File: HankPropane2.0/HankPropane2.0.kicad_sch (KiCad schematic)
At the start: 3 parts, among them X1 Badgelife_sao_connector_v169b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

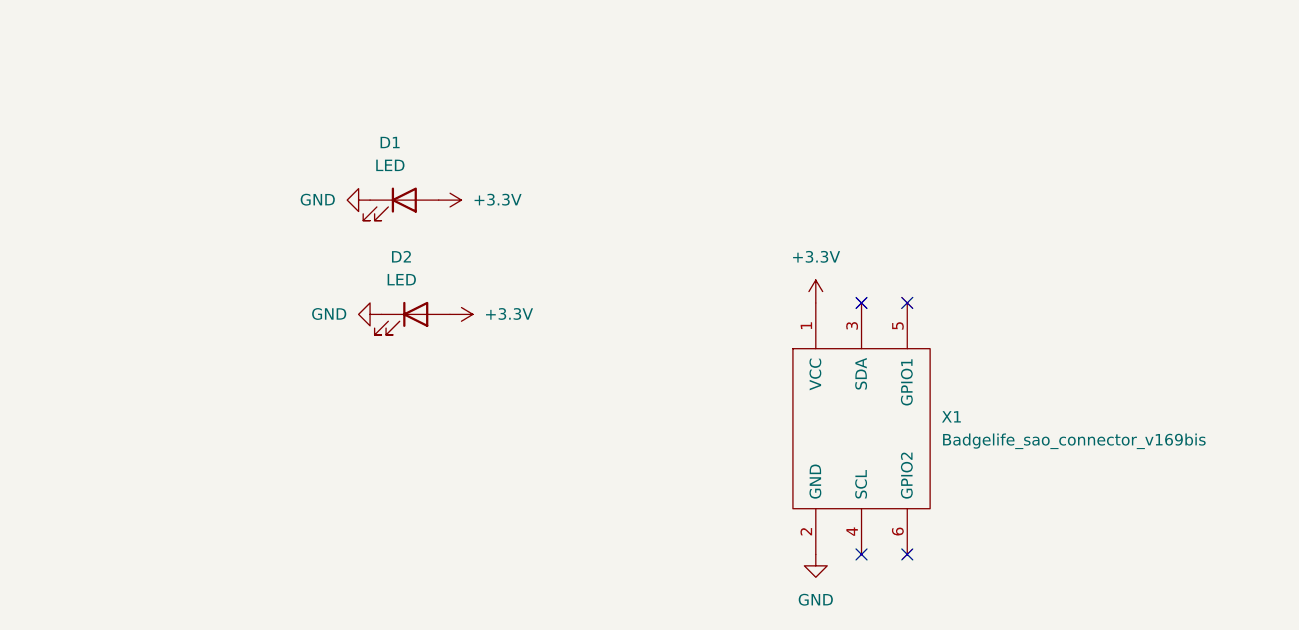
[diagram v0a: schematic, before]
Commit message: Added 68.1 ohm current limiting resistors and turbo mode jumpers
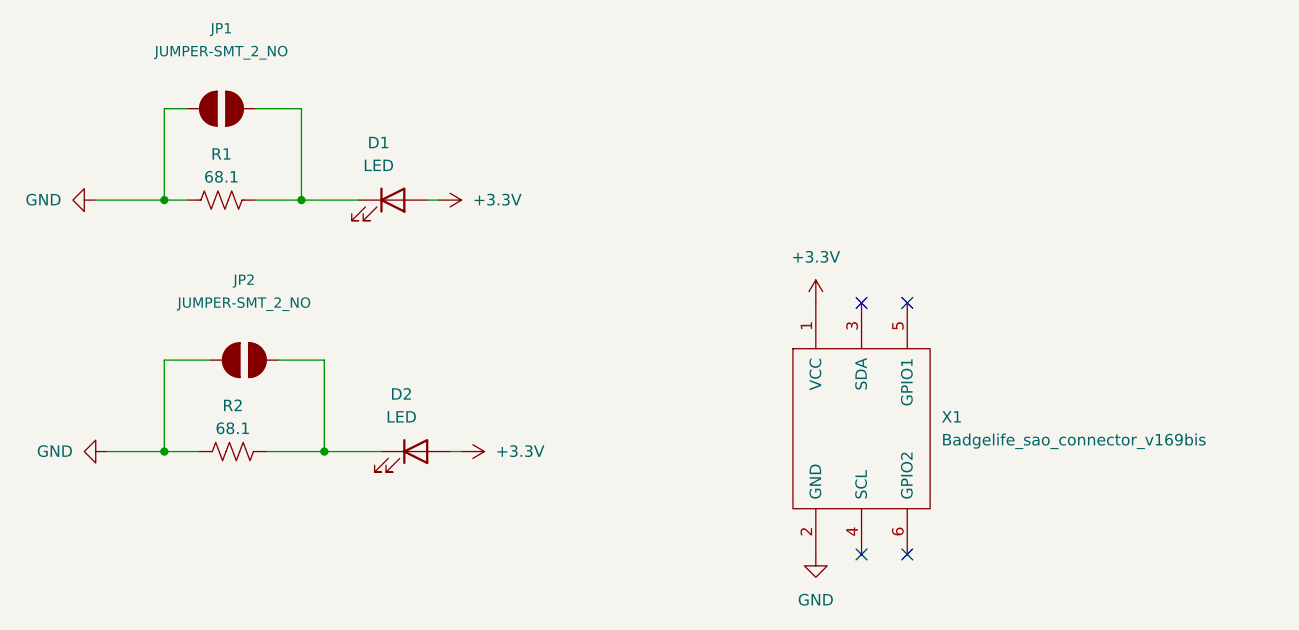
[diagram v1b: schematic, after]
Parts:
- added JP1, JP2: JUMPER-SMT_2_NO, Jumper:SolderJumper-2_P1.3mm_Open_TrianglePad1.0x1.5mm, symbol BadgePirates:JUMPER-SMT_2_NO
- added R1, R2: 68.1, Resistor_SMD:R_0805_2012Metric_Pad1.20x1.40mm_HandSolder, symbol Device:R_US
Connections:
- net GND: now also JP1.1, JP2.1, R1.1, R2.1; no longer D1.1 (K), D2.1 (K)
- new net: D2.1 (K), JP2.2, R2.2
- new net: D1.1 (K), JP1.2, R1.2
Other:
- moved on the sheet: D1, D2

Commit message: Changed resistors to 1206
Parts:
- R1, R2: footprint Resistor_SMD:R_0805_2012Metric_Pad1.20x1.40mm_HandSolder -> Resistor_SMD:R_1206_3216Metric_Pad1.30x1.75mm_HandSolder
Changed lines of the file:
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@@
       (effects (font (size 1.27 1.27)))
     )
-    (property "Footprint" "Resistor_SMD:R_0805_2012Metric_Pad1.20x1.40mm_HandSolder" (at 94.234 105.664 90)
+    (property "Footprint" "Resistor_SMD:R_1206_3216Metric_Pad1.30x1.75mm_HandSolder" (at 94.234 105.664 90)
       (effects (font (size 1.27 1.27)) hide)
     )
@@
       (effects (font (size 1.27 1.27)))
     )
-    (property "Footprint" "Resistor_SMD:R_0805_2012Metric_Pad1.20x1.40mm_HandSolder" (at 92.964 77.724 90)
+    (property "Footprint" "Resistor_SMD:R_1206_3216Metric_Pad1.30x1.75mm_HandSolder" (at 92.964 77.724 90)
       (effects (font (size 1.27 1.27)) hide)
     )
